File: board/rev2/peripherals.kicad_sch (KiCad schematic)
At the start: 11 parts, among them J7 Conn_01x09_Pin, J8 USB_C_Receptacle_USB2.0_14P, J9 Micro_SD_Card_Det1, SW4 TS-1088-AR02016

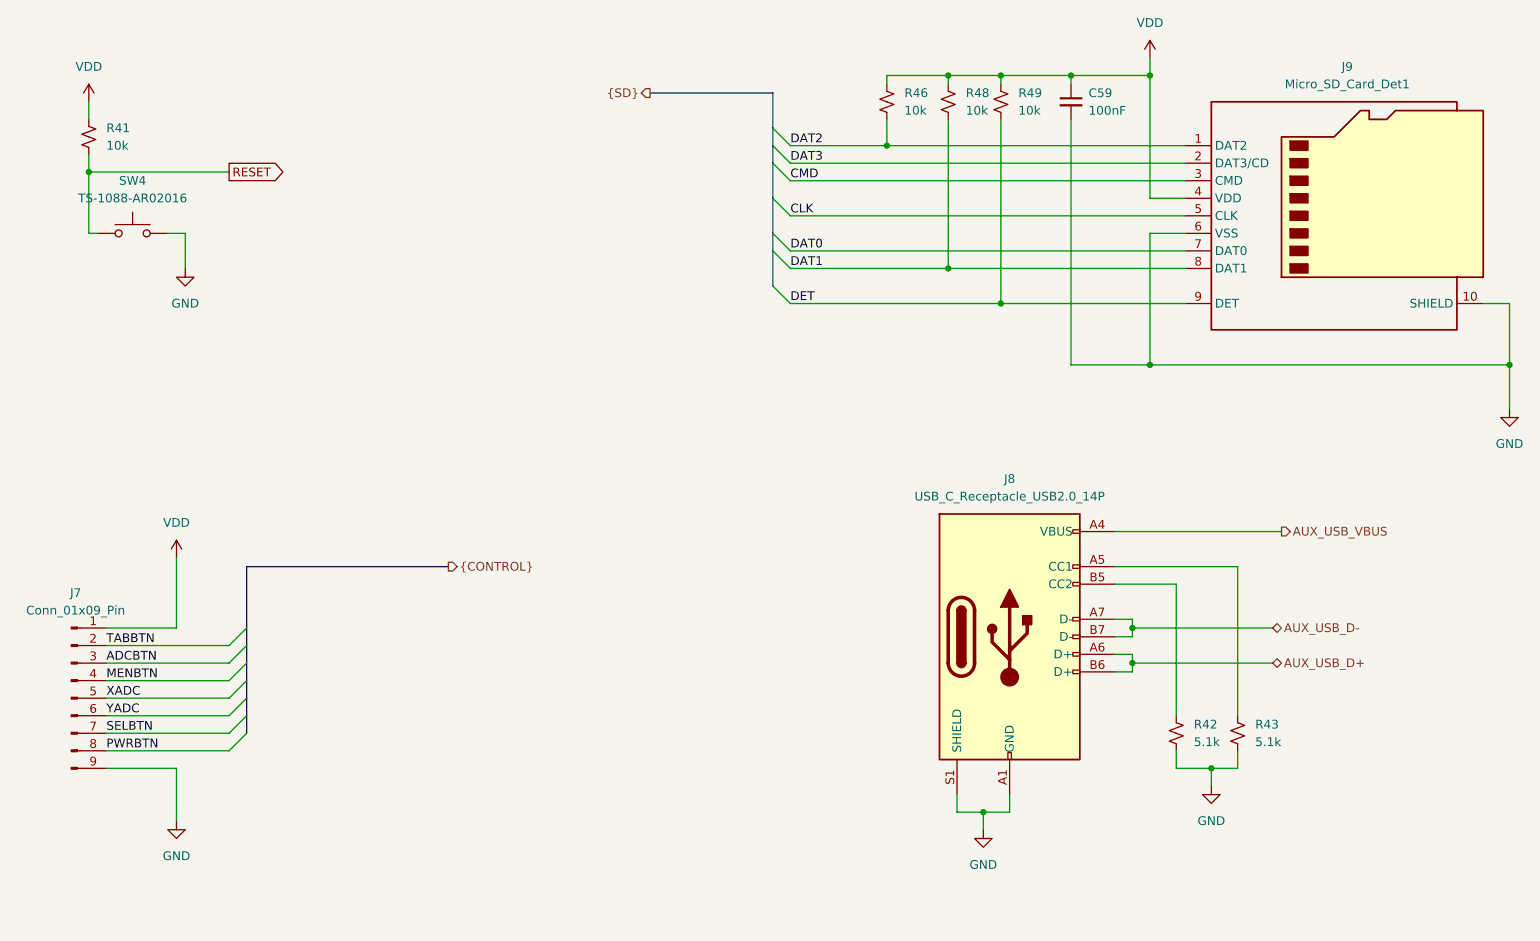
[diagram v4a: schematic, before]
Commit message: Really finish rev2 board schematic
- fix some more footprints
  - move to real SD card holder, for example
- repair part numbers
- add LCSC part refs to everything
- add even more caps to the 3.3V reg output
  - really should use an LDO but meh it should be fine

total BOM cost for 5 of them is apparently 160 CAD, or like 32 dollars
each (don't think that includes the feeder fees tho)
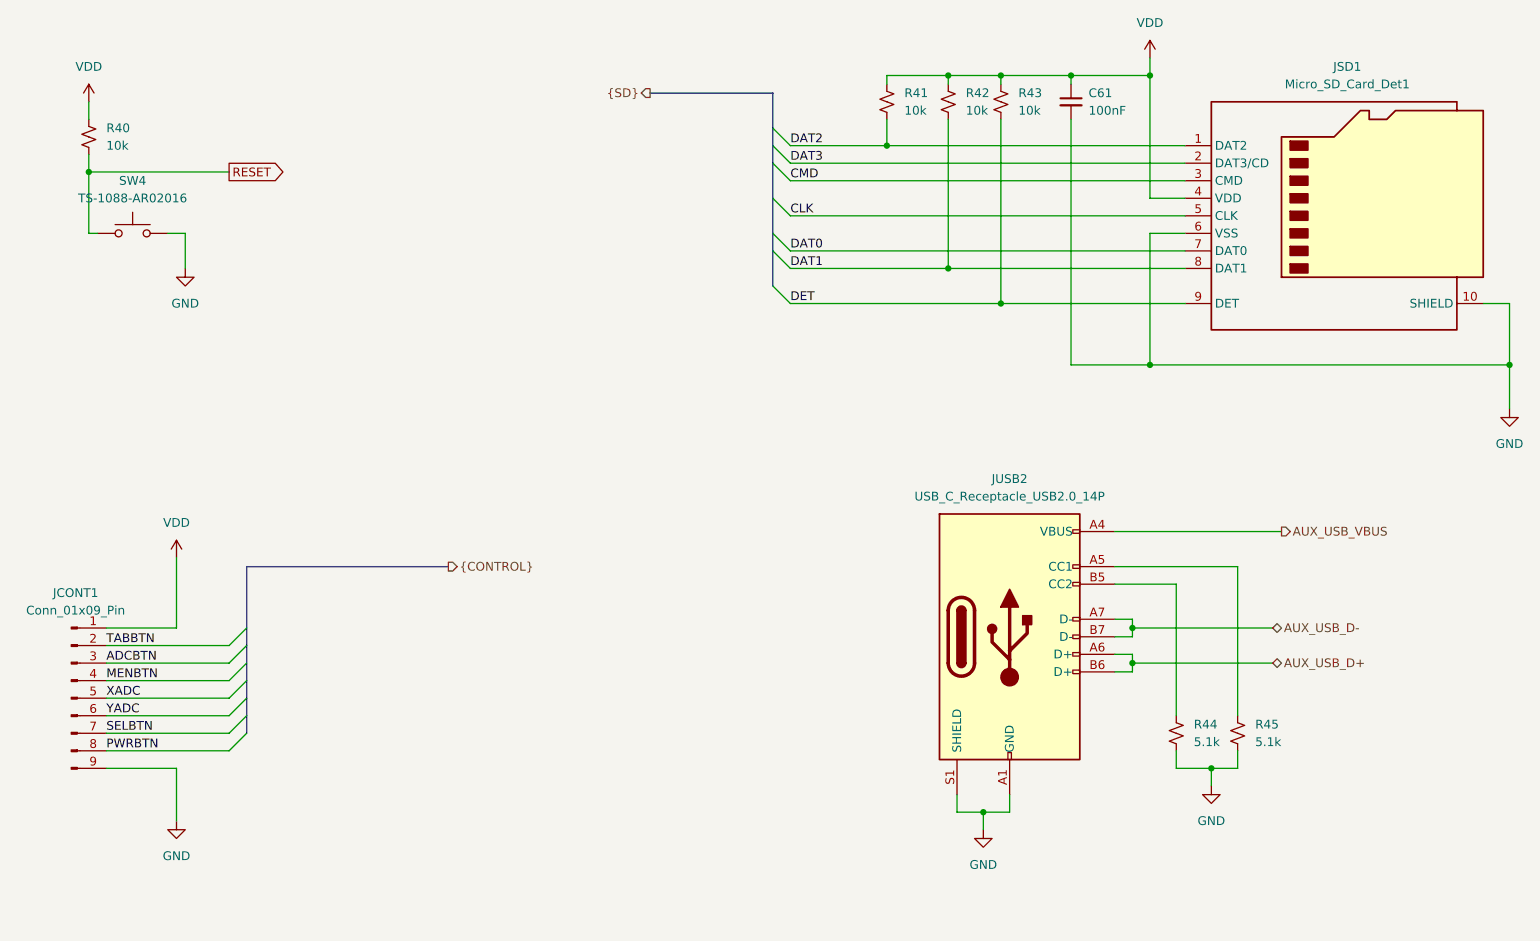
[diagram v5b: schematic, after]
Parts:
- C61: renamed from C59; LCSC (none) -> C307331
- JSD1: renamed from J9; LCSC (none) -> C720505
- JUSB2: renamed from J8; LCSC (none) -> C165948
- R40: renamed from R41; LCSC (none) -> C17414
- R41: renamed from R46; footprint (none) -> Resistor_SMD:R_0805_2012Metric; LCSC (none) -> C17414; Part (none) -> 0805W8F1002T5E
- R42: renamed from R48; footprint (none) -> Resistor_SMD:R_0805_2012Metric; LCSC (none) -> C17414; Part (none) -> 0805W8F1002T5E
- R43: renamed from R49; footprint (none) -> Resistor_SMD:R_0805_2012Metric; LCSC (none) -> C17414; Part (none) -> 0805W8F1002T5E
- R44: renamed from R42; LCSC (none) -> C23186
- R45: renamed from R43; LCSC (none) -> C23186
- SW4: LCSC (none) -> C720477
- renumbered J7 to JCONT1
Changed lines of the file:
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@@
 		(dnp no)
 		(fields_autoplaced yes)
-		(property "Reference" "R49"
+		(property "Reference" "R43"
 			(at 185.42 41.9099 0)
 			(effects
@@
 			)
 		)
-		(property "Footprint" ""
+		(property "Footprint" "Resistor_SMD:R_0805_2012Metric"
 			(at 182.88 43.18 0)
 			(effects
@@
 			)
 		)
+		(property "Part" "0805W8F1002T5E"
+			(at 182.88 43.18 0)
+			(effects
+				(font
+					(size 1.27 1.27)
+				)
+				(hide yes)
+			)
+		)
+		(property "LCSC" "C17414 "
+			(at 182.88 43.18 0)
+			(effects
+				(font
+					(size 1.27 1.27)
+				)
+				(hide yes)
+			)
+		)
 		(pin "2"
 		)
@@
 			(project "mainboard"
 				(path "/32eb05c7-b4a6-42f3-8fb3-43453631100f/802ce1c9-2668-4fe7-971c-9ba57eb1ffa9"
-					(reference "R49")
+					(reference "R43")
 					(unit 1)
 				)
@@
 			)
 		)
+		(property "LCSC" "C720477"
+			(at 57.15 62.23 0)
+			(effects
+				(font
+					(size 1.27 1.27)
+				)
+				(hide yes)
+			)
+		)
 		(pin "1"
 		)
@@
 		(dnp no)
 		(fields_autoplaced yes)
-		(property "Reference" "#PWR054"
+		(property "Reference" "#PWR055"
 			(at 204.47 40.64 0)
 			(effects
@@
 			(project ""
 				(path "/32eb05c7-b4a6-42f3-8fb3-43453631100f/802ce1c9-2668-4fe7-971c-9ba57eb1ffa9"
-					(reference "#PWR054")
+					(reference "#PWR055")
 					(unit 1)
 				)
@@
 		(dnp no)
 		(fields_autoplaced yes)
-		(property "Reference" "J9"
+		(property "Reference" "JSD1"
 			(at 233.045 38.1 0)
 			(effects
@@
 			)
 		)
+		(property "LCSC" "C720505"
+			(at 232.41 59.69 0)
+			(effects
+				(font
+					(size 1.27 1.27)
+				)
+				(hide yes)
+			)
+		)
 		(pin "1"
 		)
@@
 			(project ""
 				(path "/32eb05c7-b4a6-42f3-8fb3-43453631100f/802ce1c9-2668-4fe7-971c-9ba57eb1ffa9"
-					(reference "J9")
+					(reference "JSD1")
 					(unit 1)
 				)
@@
 		(dnp no)
 		(fields_autoplaced yes)
-		(property "Reference" "#PWR055"
+		(property "Reference" "#PWR056"
 			(at 213.36 148.59 0)
 			(effects
@@
 			(project ""
 				(path "/32eb05c7-b4a6-42f3-8fb3-43453631100f/802ce1c9-2668-4fe7-971c-9ba57eb1ffa9"
-					(reference "#PWR055")
+					(reference "#PWR056")
 					(unit 1)
 				)
@@
 		(dnp no)
 		(fields_autoplaced yes)
-		(property "Reference" "J8"
+		(property "Reference" "JUSB2"
 			(at 184.15 97.79 0)
 			(effects
@@
 			)
 		)
+		(property "LCSC" "C165948"
+			(at 184.15 120.65 0)
+			(effects
+				(font
+					(size 1.27 1.27)
+				)
+				(hide yes)
+			)
+		)
 		(pin "B6"
 		)
@@
 			(project "mainboard"
 				(path "/32eb05c7-b4a6-42f3-8fb3-43453631100f/802ce1c9-2668-4fe7-971c-9ba57eb1ffa9"
-					(reference "J8")
+					(reference "JUSB2")
 					(unit 1)
 				)
@@
 		(dnp no)
 		(fields_autoplaced yes)
-		(property "Reference" "#PWR053"
+		(property "Reference" "#PWR054"
 			(at 180.34 154.94 0)
 			(effects
@@
 			(project "mainboard"
 				(path "/32eb05c7-b4a6-42f3-8fb3-43453631100f/802ce1c9-2668-4fe7-971c-9ba57eb1ffa9"
-					(reference "#PWR053")
+					(reference "#PWR054")
 					(unit 1)
 				)
@@
 		(dnp no)
 		(fields_autoplaced yes)
-		(property "Reference" "#PWR049"
+		(property "Reference" "#PWR050"
 			(at 50.8 46.99 0)
 			(effects
@@
 			(project "mainboard"
 				(path "/32eb05c7-b4a6-42f3-8fb3-43453631100f/802ce1c9-2668-4fe7-971c-9ba57eb1ffa9"
-					(reference "#PWR049")
+					(reference "#PWR050")
 					(unit 1)
 				)
@@
 		(dnp no)
 		(fields_autoplaced yes)
-		(property "Reference" "R43"
+		(property "Reference" "R45"
 			(at 219.71 133.3499 0)
 			(effects
@@
 			)
 		)
+		(property "LCSC" "C23186"
+			(at 217.17 134.62 0)
+			(effects
+				(font
+					(size 1.27 1.27)
+				)
+				(hide yes)
+			)
+		)
 		(pin "2"
 		)
@@
 			(project ""
 				(path "/32eb05c7-b4a6-42f3-8fb3-43453631100f/802ce1c9-2668-4fe7-971c-9ba57eb1ffa9"
-					(reference "R43")
+					(reference "R45")
 					(unit 1)
 				)
@@
 		(dnp no)
 		(fields_autoplaced yes)
-		(property "Reference" "C59"
+		(property "Reference" "C61"
 			(at 195.58 41.9162 0)
 			(effects
@@
 			)
 		)
+		(property "LCSC" "C307331 "
+			(at 193.04 43.18 0)
+			(effects
+				(font
+					(size 1.27 1.27)
+				)
+				(hide yes)
+			)
+		)
 		(pin "2"
 		)
@@
 			(project ""
 				(path "/32eb05c7-b4a6-42f3-8fb3-43453631100f/802ce1c9-2668-4fe7-971c-9ba57eb1ffa9"
-					(reference "C59")
+					(reference "C61")
 					(unit 1)
 				)
@@
 		(dnp no)
 		(fields_autoplaced yes)
-		(property "Reference" "#PWR050"
+		(property "Reference" "#PWR051"
 			(at 63.5 113.03 0)
 			(effects
@@
 			(project ""
 				(path "/32eb05c7-b4a6-42f3-8fb3-43453631100f/802ce1c9-2668-4fe7-971c-9ba57eb1ffa9"
-					(reference "#PWR050")
+					(reference "#PWR051")
 					(unit 1)
 				)
@@
 		(dnp no)
 		(fields_autoplaced yes)
-		(property "Reference" "#PWR052"
+		(property "Reference" "#PWR053"
 			(at 64.77 73.66 0)
 			(effects
@@
 			(project ""
 				(path "/32eb05c7-b4a6-42f3-8fb3-43453631100f/802ce1c9-2668-4fe7-971c-9ba57eb1ffa9"
-					(reference "#PWR052")
+					(reference "#PWR053")
 					(unit 1)
 				)
@@
 		(dnp no)
 		(fields_autoplaced yes)
-		(property "Reference" "R41"
+		(property "Reference" "R40"
 			(at 53.34 46.9899 0)
 			(effects
@@
 			)
 		)
+		(property "LCSC" "C17414 "
+			(at 50.8 48.26 0)
+			(effects
+				(font
+					(size 1.27 1.27)
+				)
+				(hide yes)
+			)
+		)
 		(pin "1"
 		)
@@
 			(project ""
 				(path "/32eb05c7-b4a6-42f3-8fb3-43453631100f/802ce1c9-2668-4fe7-971c-9ba57eb1ffa9"
-					(reference "R41")
+					(reference "R40")
 					(unit 1)
 				)
@@
 		(dnp no)
 		(fields_autoplaced yes)
-		(property "Reference" "#PWR056"
+		(property "Reference" "#PWR057"
 			(at 256.54 93.98 0)
 			(effects
@@
 			(project ""
 				(path "/32eb05c7-b4a6-42f3-8fb3-43453631100f/802ce1c9-2668-4fe7-971c-9ba57eb1ffa9"
-					(reference "#PWR056")
+					(reference "#PWR057")
 					(unit 1)
 				)
@@
 		(dnp no)
 		(fields_autoplaced yes)
-		(property "Reference" "R48"
+		(property "Reference" "R42"
 			(at 177.8 41.9099 0)
 			(effects
@@
 			)
 		)
-		(property "Footprint" ""
+		(property "Footprint" "Resistor_SMD:R_0805_2012Metric"
 			(at 175.26 43.18 0)
 			(effects
@@
 			)
 		)
+		(property "Part" "0805W8F1002T5E"
+			(at 175.26 43.18 0)
+			(effects
+				(font
+					(size 1.27 1.27)
+				)
+				(hide yes)
+			)
+		)
+		(property "LCSC" "C17414 "
+			(at 175.26 43.18 0)
+			(effects
+				(font
+					(size 1.27 1.27)
+				)
+				(hide yes)
+			)
+		)
 		(pin "2"
 		)
@@
 			(project ""
 				(path "/32eb05c7-b4a6-42f3-8fb3-43453631100f/802ce1c9-2668-4fe7-971c-9ba57eb1ffa9"
-					(reference "R48")
+					(reference "R42")
 					(unit 1)
 				)
@@
 		(dnp no)
 		(fields_autoplaced yes)
-		(property "Reference" "R42"
+		(property "Reference" "R44"
 			(at 210.82 133.3499 0)
 			(effects
@@
 			)
 		)
+		(property "LCSC" "C23186"
+			(at 208.28 134.62 0)
+			(effects
+				(font
+					(size 1.27 1.27)
+				)
+				(hide yes)
+			)
+		)
 		(pin "2"
 		)
@@
 			(project ""
 				(path "/32eb05c7-b4a6-42f3-8fb3-43453631100f/802ce1c9-2668-4fe7-971c-9ba57eb1ffa9"
-					(reference "R42")
+					(reference "R44")
 					(unit 1)
 				)
@@
 		(dnp no)
 		(fields_autoplaced yes)
-		(property "Reference" "R46"
+		(property "Reference" "R41"
 			(at 168.91 41.9099 0)
 			(effects
@@
 			)
 		)
-		(property "Footprint" ""
+		(property "Footprint" "Resistor_SMD:R_0805_2012Metric"
 			(at 166.37 43.18 0)
 			(effects
@@
 			)
 		)
+		(property "Part" "0805W8F1002T5E"
+			(at 166.37 43.18 0)
+			(effects
+				(font
+					(size 1.27 1.27)
+				)
+				(hide yes)
+			)
+		)
+		(property "LCSC" "C17414 "
+			(at 166.37 43.18 0)
+			(effects
+				(font
+					(size 1.27 1.27)
+				)
+				(hide yes)
+			)
+		)
 		(pin "2"
 		)
@@
 			(project ""
 				(path "/32eb05c7-b4a6-42f3-8fb3-43453631100f/802ce1c9-2668-4fe7-971c-9ba57eb1ffa9"
-					(reference "R46")
+					(reference "R41")
 					(unit 1)
 				)
@@
 		(dnp no)
 		(fields_autoplaced yes)
-		(property "Reference" "J7"
+		(property "Reference" "JCONT1"
 			(at 48.895 114.3 0)
 			(effects
@@
 			)
 		)
+		(property "LCSC" ""
+			(at 48.26 129.54 0)
+			(effects
+				(font
+					(size 1.27 1.27)
+				)
+				(hide yes)
+			)
+		)
 		(pin "4"
 		)
@@
 			(project ""
 				(path "/32eb05c7-b4a6-42f3-8fb3-43453631100f/802ce1c9-2668-4fe7-971c-9ba57eb1ffa9"
-					(reference "J7")
+					(reference "JCONT1")
 					(unit 1)
 				)
@@
 		(dnp no)
 		(fields_autoplaced yes)
-		(property "Reference" "#PWR051"
+		(property "Reference" "#PWR052"
 			(at 63.5 153.67 0)
 			(effects
@@
 			(project ""
 				(path "/32eb05c7-b4a6-42f3-8fb3-43453631100f/802ce1c9-2668-4fe7-971c-9ba57eb1ffa9"
-					(reference "#PWR051")
-					(unit 1)
-				)
+					(reference "#PWR052")
+					(unit 1)
+				)

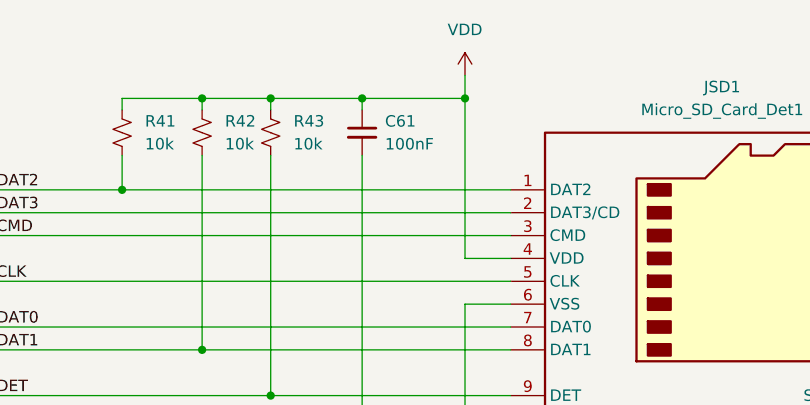
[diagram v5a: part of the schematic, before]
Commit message: Start board
add a few extra bypass caps too, and swap some pins on the USB mux

i forgot to add a bypass cap on the tpd6s so that also needs to happen

truly 63 capacitors is not enough
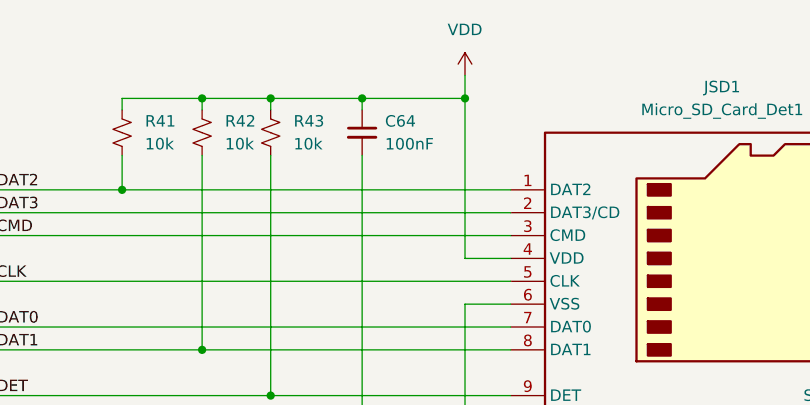
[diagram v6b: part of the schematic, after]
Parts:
- renumbered C61 to C64
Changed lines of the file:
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@@
 		(dnp no)
 		(fields_autoplaced yes)
-		(property "Reference" "#PWR055"
+		(property "Reference" "#PWR056"
 			(at 204.47 40.64 0)
 			(effects
@@
 			(project ""
 				(path "/32eb05c7-b4a6-42f3-8fb3-43453631100f/802ce1c9-2668-4fe7-971c-9ba57eb1ffa9"
-					(reference "#PWR055")
+					(reference "#PWR056")
 					(unit 1)
 				)
@@
 		(dnp no)
 		(fields_autoplaced yes)
-		(property "Reference" "#PWR056"
+		(property "Reference" "#PWR057"
 			(at 213.36 148.59 0)
 			(effects
@@
 			(project ""
 				(path "/32eb05c7-b4a6-42f3-8fb3-43453631100f/802ce1c9-2668-4fe7-971c-9ba57eb1ffa9"
-					(reference "#PWR056")
+					(reference "#PWR057")
 					(unit 1)
 				)
@@
 		(dnp no)
 		(fields_autoplaced yes)
-		(property "Reference" "#PWR054"
+		(property "Reference" "#PWR055"
 			(at 180.34 154.94 0)
 			(effects
@@
 			(project "mainboard"
 				(path "/32eb05c7-b4a6-42f3-8fb3-43453631100f/802ce1c9-2668-4fe7-971c-9ba57eb1ffa9"
-					(reference "#PWR054")
+					(reference "#PWR055")
 					(unit 1)
 				)
@@
 		(dnp no)
 		(fields_autoplaced yes)
-		(property "Reference" "#PWR050"
+		(property "Reference" "#PWR051"
 			(at 50.8 46.99 0)
 			(effects
@@
 			(project "mainboard"
 				(path "/32eb05c7-b4a6-42f3-8fb3-43453631100f/802ce1c9-2668-4fe7-971c-9ba57eb1ffa9"
-					(reference "#PWR050")
+					(reference "#PWR051")
 					(unit 1)
 				)
@@
 		(dnp no)
 		(fields_autoplaced yes)
-		(property "Reference" "C61"
+		(property "Reference" "C64"
 			(at 195.58 41.9162 0)
 			(effects
@@
 			(project ""
 				(path "/32eb05c7-b4a6-42f3-8fb3-43453631100f/802ce1c9-2668-4fe7-971c-9ba57eb1ffa9"
-					(reference "C61")
+					(reference "C64")
 					(unit 1)
 				)
@@
 		(dnp no)
 		(fields_autoplaced yes)
-		(property "Reference" "#PWR051"
+		(property "Reference" "#PWR052"
 			(at 63.5 113.03 0)
 			(effects
@@
 			(project ""
 				(path "/32eb05c7-b4a6-42f3-8fb3-43453631100f/802ce1c9-2668-4fe7-971c-9ba57eb1ffa9"
-					(reference "#PWR051")
+					(reference "#PWR052")
 					(unit 1)
 				)
@@
 		(dnp no)
 		(fields_autoplaced yes)
-		(property "Reference" "#PWR053"
+		(property "Reference" "#PWR054"
 			(at 64.77 73.66 0)
 			(effects
@@
 			(project ""
 				(path "/32eb05c7-b4a6-42f3-8fb3-43453631100f/802ce1c9-2668-4fe7-971c-9ba57eb1ffa9"
-					(reference "#PWR053")
+					(reference "#PWR054")
 					(unit 1)
 				)
@@
 		(dnp no)
 		(fields_autoplaced yes)
-		(property "Reference" "#PWR057"
+		(property "Reference" "#PWR058"
 			(at 256.54 93.98 0)
 			(effects
@@
 			(project ""
 				(path "/32eb05c7-b4a6-42f3-8fb3-43453631100f/802ce1c9-2668-4fe7-971c-9ba57eb1ffa9"
-					(reference "#PWR057")
+					(reference "#PWR058")
 					(unit 1)
 				)
@@
 		(dnp no)
 		(fields_autoplaced yes)
-		(property "Reference" "#PWR052"
+		(property "Reference" "#PWR053"
 			(at 63.5 153.67 0)
 			(effects
@@
 			(project ""
 				(path "/32eb05c7-b4a6-42f3-8fb3-43453631100f/802ce1c9-2668-4fe7-971c-9ba57eb1ffa9"
-					(reference "#PWR052")
-					(unit 1)
-				)
+					(reference "#PWR053")
+					(unit 1)
+				)

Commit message: Finish board rev2
woo another pcb
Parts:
- added C74: 1uF, Capacitor_SMD:C_0603_1608Metric, symbol Device:C_Small
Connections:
- net GND: now also C74.2
- net RESET: now also C74.1
- net CLK renamed SDCLK
